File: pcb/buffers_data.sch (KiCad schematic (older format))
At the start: 8 parts

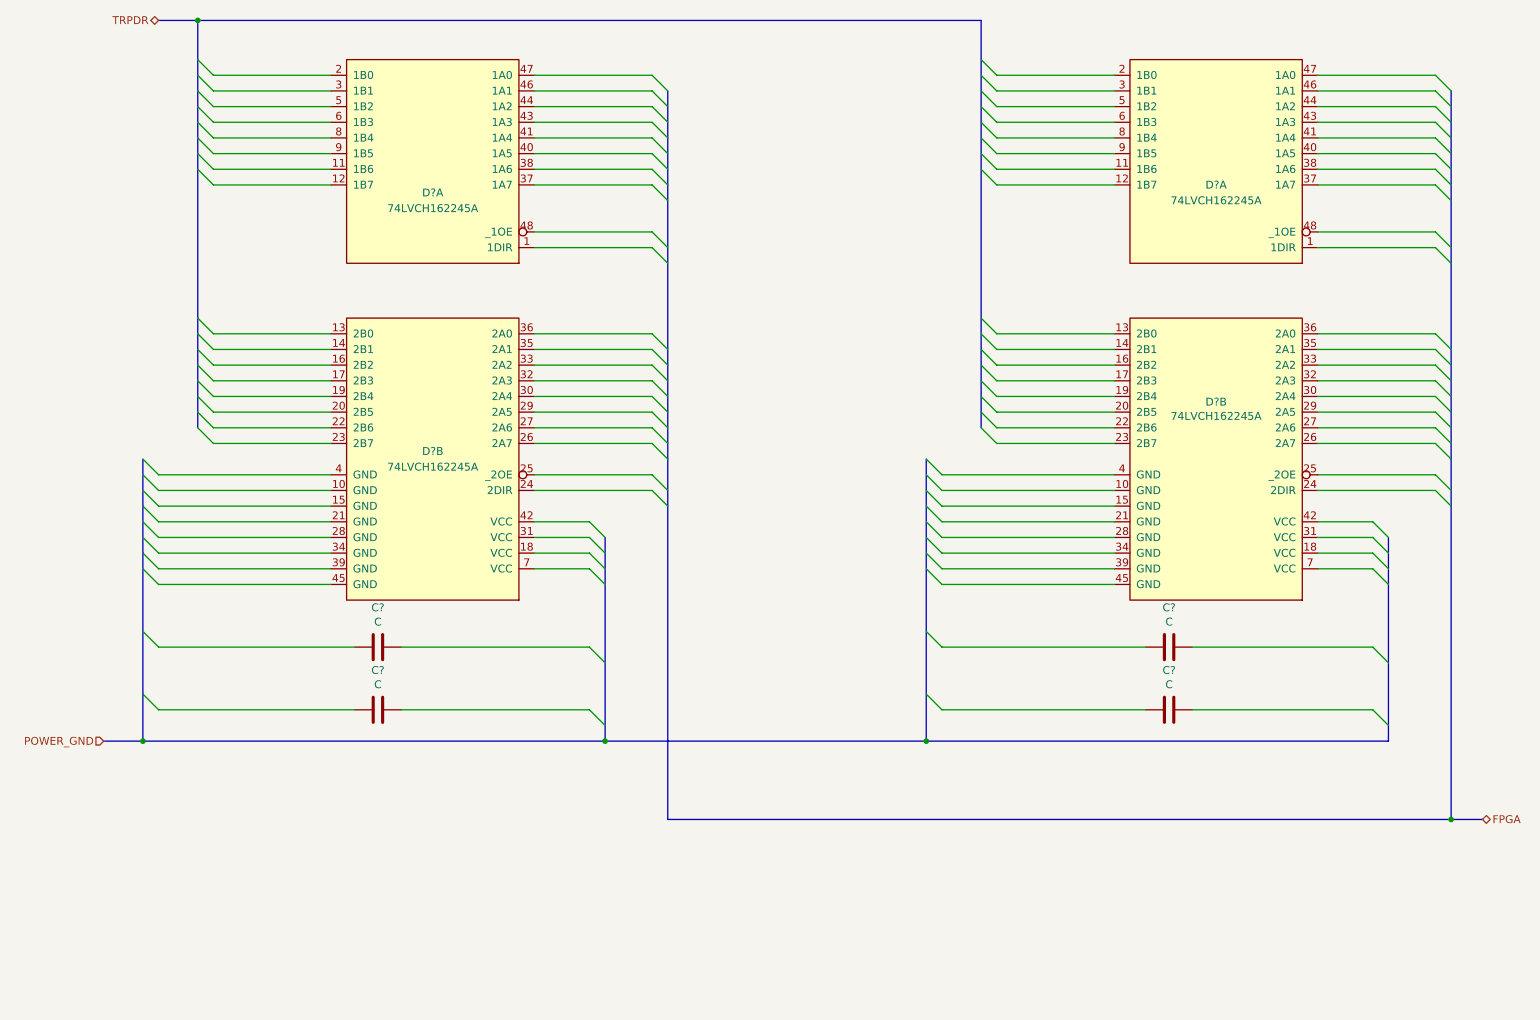
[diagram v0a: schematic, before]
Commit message: buffer section finished, audio moved to expansion connector
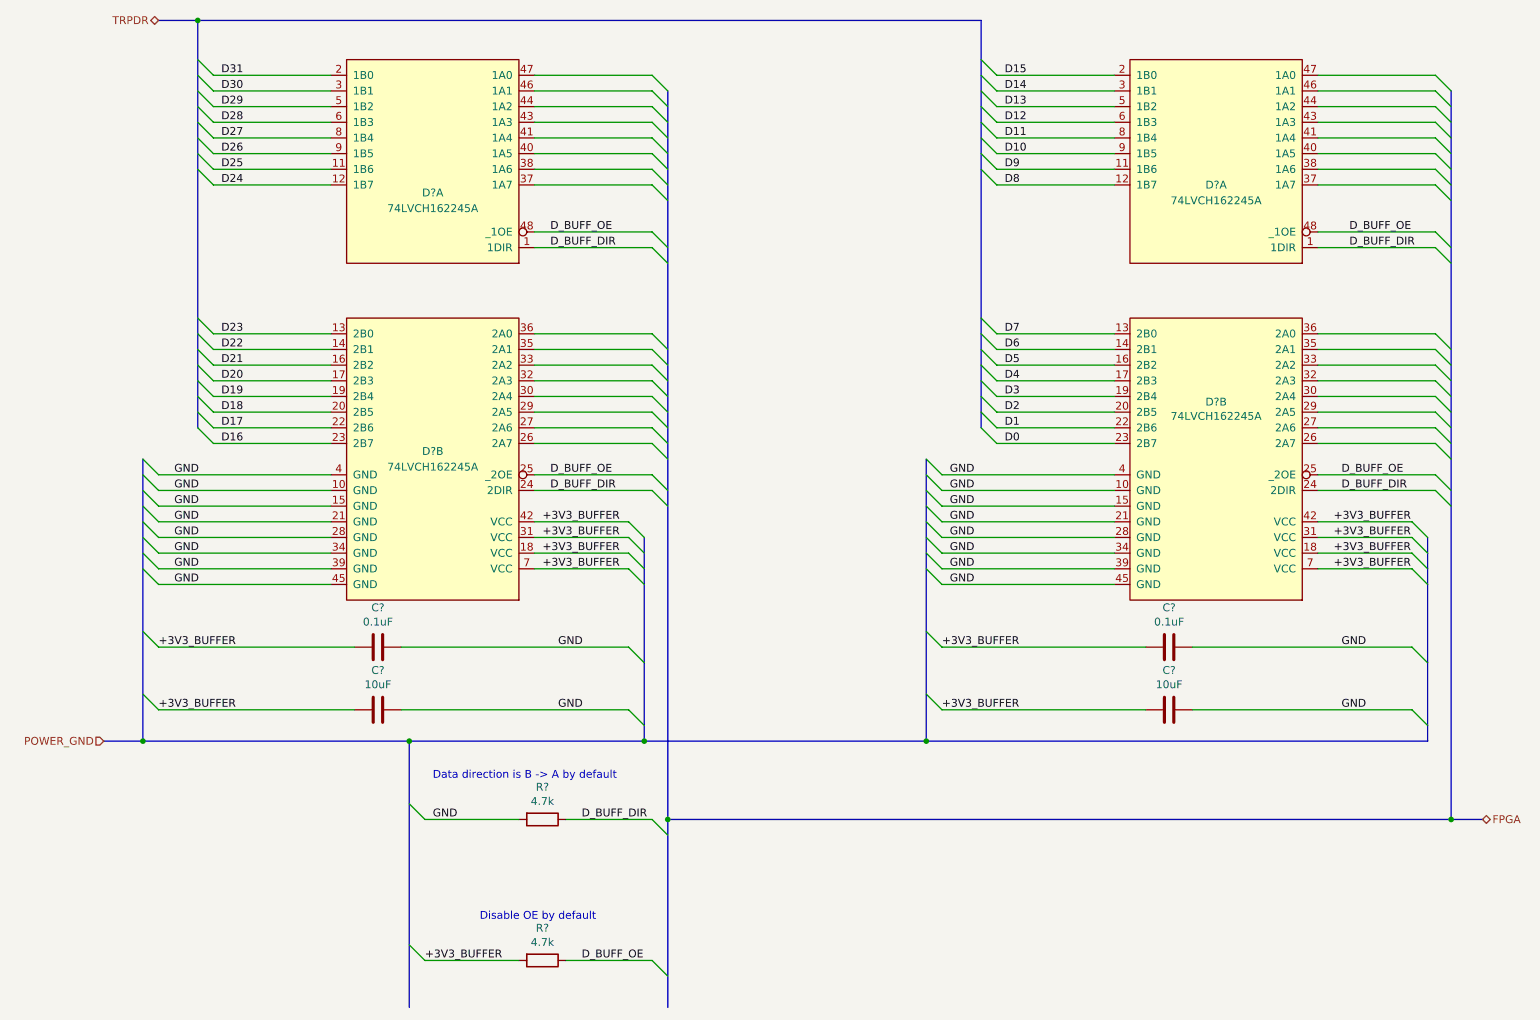
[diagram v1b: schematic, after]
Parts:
- added R? (x2): 4.7k, symbol Device:R
- C? (x2): value C -> 10uF
- C? (x2): value C -> 0.1uF
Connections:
- net D_BUFF_DIR: now reaches D?.1 (1DIR)
- net D_BUFF_DIR: now also D?.1 (1DIR), D?.24 (2DIR), D?.24 (2DIR), R?.1
- net D25: now reaches D?.11 (1B6)
- net D24: now reaches D?.12 (1B7)
- net D31: now reaches D?.2 (1B0)
- net D30: now reaches D?.3 (1B1)
- net D_BUFF_OE: now reaches D?.48 (_1OE)
- net D_BUFF_OE: now also D?.25 (_2OE), D?.25 (_2OE), D?.48 (_1OE), R?.1
- net D29: now reaches D?.5 (1B2)
- net D28: now reaches D?.6 (1B3)
- net D27: now reaches D?.8 (1B4)
- net D26: now reaches D?.9 (1B5)
- net GND: now reaches D?.10 (GND)
- net GND: now also C?.2, C?.2, C?.2, C?.2, D?.10 (GND), D?.15 (GND), D?.15 (GND), D?.21 (GND), D?.21 (GND), D?.28 (GND), D?.28 (GND), D?.34 (GND), D?.34 (GND), D?.39 (GND), D?.39 (GND), D?.4 (GND), D?.4 (GND), D?.45 (GND), D?.45 (GND), R?.2
- net D23: now reaches D?.13 (2B0)
- net D22: now reaches D?.14 (2B1)
- net D21: now reaches D?.16 (2B2)
- net D20: now reaches D?.17 (2B3)
- net +3V3_BUFFER: now reaches D?.18 (VCC)
- net +3V3_BUFFER: now also C?.1, C?.1, C?.1, C?.1, D?.18 (VCC), D?.31 (VCC), D?.31 (VCC), D?.42 (VCC), D?.42 (VCC), D?.7 (VCC), D?.7 (VCC), R?.2
- net D19: now reaches D?.19 (2B4)
- net D18: now reaches D?.20 (2B5)
- net D17: now reaches D?.22 (2B6)
- net D16: now reaches D?.23 (2B7)
- net D9: now reaches D?.11 (1B6)
- net D8: now reaches D?.12 (1B7)
- net D15: now reaches D?.2 (1B0)
- net D14: now reaches D?.3 (1B1)
- net D13: now reaches D?.5 (1B2)
- net D12: now reaches D?.6 (1B3)
- net D11: now reaches D?.8 (1B4)
- net D10: now reaches D?.9 (1B5)
- net D7: now reaches D?.13 (2B0)
- net D6: now reaches D?.14 (2B1)
- net D5: now reaches D?.16 (2B2)
- net D4: now reaches D?.17 (2B3)
- net D3: now reaches D?.19 (2B4)
- net D2: now reaches D?.20 (2B5)
- net D1: now reaches D?.22 (2B6)
- net D0: now reaches D?.23 (2B7)
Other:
- note added: "Data direction is B -> A by default"
- note added: "Disable OE by default"
